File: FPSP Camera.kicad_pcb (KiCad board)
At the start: 4 copper layers, 85.7 x 31.1 mm, 73 parts, among them J1 Conn_01x24_Socket, J2 Conn_01x02, J3 Conn_02x07_Counter_Clockwise, J4 Conn_02x07_Counter_Clockwise, U1 ICM-45686, U3 RP2350_60QFN, U4 TLV75533PDRV, U5 TLV73328PDRV, U6 TLV73315PDRV, Y1 SiT8008xx-1x-xxE

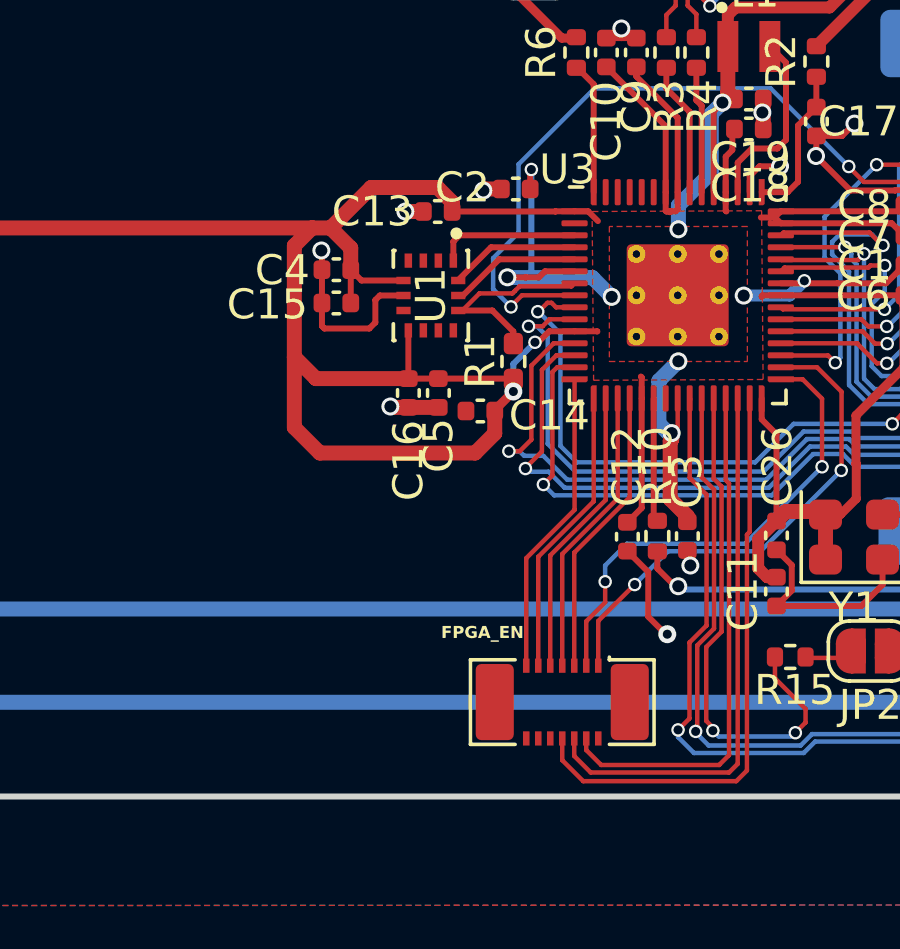
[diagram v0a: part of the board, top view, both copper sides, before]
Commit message: GPIO_1 added
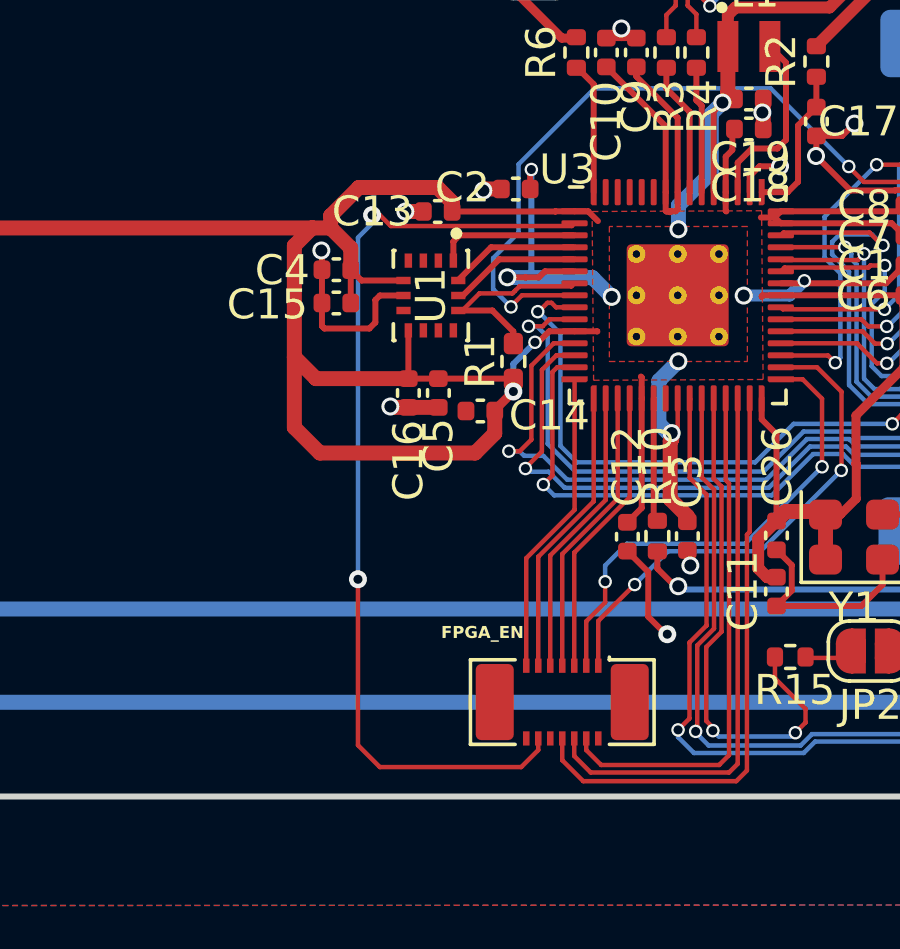
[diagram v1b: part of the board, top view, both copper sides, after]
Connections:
- J4 pad 12: unconnected-(J4-Pin_12-Pad12) -> POSITION_OUT_1
- J4 pad 3: POSITION_OUT_1 -> FPGA_CTRL
- U3 pad 2: /GPIO0_1 -> POSITION_OUT_1
- U3 pad 31: POSITION_OUT_1 -> FPGA_CTRL
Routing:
- net FPGA_CTRL: track 0.00 -> 16.1 mm, vias 0 -> 2
- net POSITION_OUT_1: track 16.1 -> 31.7 mm
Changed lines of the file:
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@@
 			(layers "F.Cu" "F.Mask" "F.Paste")
 			(roundrect_rratio 0.25)
-			(net "/GPIO0_1")
+			(net "POSITION_OUT_1")
 			(pinfunction "GPIO0_2")
 			(pintype "bidirectional")
@@
 			(chamfer_ratio 0.25)
 			(chamfer bottom_left)
-			(net "POSITION_OUT_1")
+			(net "FPGA_CTRL")
 			(pinfunction "GPIO19_31")
 			(pintype "bidirectional")
@@
 			(size 0.22 0.475)
 			(layers "F.Cu" "F.Mask" "F.Paste")
-			(net "POSITION_OUT_1")
+			(net "FPGA_CTRL")
 			(pinfunction "Pin_3_3")
 			(pintype "passive")
@@
 			(size 0.22 0.475)
 			(layers "F.Cu" "F.Mask" "F.Paste")
-			(net "unconnected-(J4-Pin_12-Pad12)")
+			(net "POSITION_OUT_1")
 			(pinfunction "Pin_12_12")
-			(pintype "passive+no_connect")
+			(pintype "passive")
 		)
 		(pad "13" smd rect
@@
 	)
 	(segment
+		(start 56.272265 26.719144)
+		(end 58.892264 26.719144)
+		(width 0.5)
+		(layer "F.Cu")
+		(net "+3.3V")
+	)
+	(segment
 		(start 66.622265 27.519144)
 		(end 66.645231 27.54211)
@@
 	)
 	(segment
+		(start 58.892264 26.719144)
+		(end 59.382265 27.209145)
+		(width 0.5)
+		(layer "F.Cu")
+		(net "+3.3V")
+	)
+	(segment
 		(start 58.922265 33.089144)
 		(end 57.922265 33.089144)
@@
 	)
 	(segment
-		(start 59.382265 27.209145)
-		(end 59.382265 27.519144)
-		(width 0.5)
-		(layer "F.Cu")
-		(net "+3.3V")
-	)
-	(segment
 		(start 73.412265 20.119144)
 		(end 71.522265 22.009144)
@@
 	)
 	(segment
-		(start 56.68234 26.719144)
-		(end 58.892264 26.719144)
-		(width 0.5)
-		(layer "F.Cu")
-		(net "+3.3V")
-	)
-	(segment
-		(start 55.33334 28.068144)
-		(end 56.68234 26.719144)
-		(width 0.5)
-		(layer "F.Cu")
-		(net "+3.3V")
-	)
-	(segment
 		(start 39.222265 30.869144)
 		(end 39.222265 30.876644)
@@
 	)
 	(segment
-		(start 58.892264 26.719144)
-		(end 59.382265 27.209145)
-		(width 0.5)
-		(layer "F.Cu")
-		(net "+3.3V")
-	)
-	(segment
 		(start 31.122265 30.019144)
 		(end 31.472265 29.669144)
@@
 	)
 	(segment
+		(start 59.382265 27.209145)
+		(end 59.382265 27.519144)
+		(width 0.5)
+		(layer "F.Cu")
+		(net "+3.3V")
+	)
+	(segment
 		(start 62.822265 27.519144)
 		(end 59.382265 27.519144)
@@
 	)
 	(segment
+		(start 55.33334 28.068144)
+		(end 55.33334 27.658069)
+		(width 0.5)
+		(layer "F.Cu")
+		(net "+3.3V")
+	)
+	(segment
 		(start 70.3375 27.5125)
 		(end 70.130856 27.719144)
@@
 	)
 	(segment
+		(start 55.33334 27.658069)
+		(end 56.272265 26.719144)
+		(width 0.5)
+		(layer "F.Cu")
+		(net "+3.3V")
+	)
+	(segment
 		(start 80.422265 24.769144)
 		(end 80.422265 21.869144)
@@
 	)
 	(segment
-		(start 64.482265 39.859144)
-		(end 64.482265 40.549144)
+		(start 56.242265 39.779144)
+		(end 56.242265 45.309144)
 		(width 0.15)
 		(layer "F.Cu")
@@
 	)
 	(segment
-		(start 64.482265 40.549144)
-		(end 63.852265 41.179144)
+		(start 56.712265 27.639144)
+		(end 56.972265 27.639144)
 		(width 0.15)
 		(layer "F.Cu")
@@
 	)
 	(segment
-		(start 70.3375 33.1125)
-		(end 71.065621 33.1125)
+		(start 61.684765 46.039144)
+		(end 62.252265 45.471644)
 		(width 0.15)
 		(layer "F.Cu")
@@
 	)
 	(segment
-		(start 71.065621 33.1125)
-		(end 71.712265 33.759144)
+		(start 62.252265 45.471644)
+		(end 62.252265 45.084144)
 		(width 0.15)
 		(layer "F.Cu")
@@
 	)
 	(segment
-		(start 63.852265 41.179144)
-		(end 63.852265 42.659144)
+		(start 63.370856 28.004144)
+		(end 63.4625 27.9125)
 		(width 0.15)
 		(layer "F.Cu")
@@
 	)
 	(segment
-		(start 71.712265 33.759144)
-		(end 71.712265 36.029144)
+		(start 56.242265 45.309144)
+		(end 56.972265 46.039144)
+		(width 0.15)
+		(layer "F.Cu")
+		(net "POSITION_OUT_1")
+	)
+	(segment
+		(start 56.972265 46.039144)
+		(end 61.684765 46.039144)
+		(width 0.15)
+		(layer "F.Cu")
+		(net "POSITION_OUT_1")
+	)
+	(segment
+		(start 56.972265 27.639144)
+		(end 57.337265 28.004144)
+		(width 0.15)
+		(layer "F.Cu")
+		(net "POSITION_OUT_1")
+	)
+	(segment
+		(start 57.337265 28.004144)
+		(end 63.370856 28.004144)
 		(width 0.15)
 		(layer "F.Cu")
@@
 	)
 	(via
-		(at 64.482265 39.859144)
-		(size 0.45)
+		(at 56.242265 39.779144)
+		(size 0.6)
 		(drill 0.3)
 		(layers "F.Cu" "B.Cu")
@@
 	)
 	(via
-		(at 71.712265 36.029144)
-		(size 0.45)
+		(at 56.712265 27.639144)
+		(size 0.6)
 		(drill 0.3)
 		(layers "F.Cu" "B.Cu")
@@
 	)
 	(segment
-		(start 69.147265 38.594144)
-		(end 65.207265 38.594144)
+		(start 56.712265 27.639144)
+		(end 56.712265 27.919144)
 		(width 0.15)
 		(layer "B.Cu")
@@
 	)
 	(segment
-		(start 71.712265 36.029144)
-		(end 69.147265 38.594144)
+		(start 56.242265 28.389144)
+		(end 56.242265 39.779144)
 		(width 0.15)
 		(layer "B.Cu")
@@
 	)
 	(segment
-		(start 65.207265 38.594144)
-		(end 64.482265 39.319144)
-		(width 0.15)
-		(layer "B.Cu")
-		(net "POSITION_OUT_1")
-	)
-	(segment
-		(start 64.482265 39.319144)
-		(end 64.482265 39.859144)
+		(start 56.712265 27.919144)
+		(end 56.242265 28.389144)
 		(width 0.15)
 		(layer "B.Cu")
@@
 		(net "DGND")
 	)
+	(segment
+		(start 64.482265 39.859144)
+		(end 64.482265 40.549144)
+		(width 0.15)
+		(layer "F.Cu")
+		(net "FPGA_CTRL")
+	)
+	(segment
+		(start 64.482265 40.549144)
+		(end 63.852265 41.179144)
+		(width 0.15)
+		(layer "F.Cu")
+		(net "FPGA_CTRL")
+	)
+	(segment
+		(start 70.3375 33.1125)
+		(end 71.065621 33.1125)
+		(width 0.15)
+		(layer "F.Cu")
+		(net "FPGA_CTRL")
+	)
+	(segment
+		(start 71.065621 33.1125)
+		(end 71.712265 33.759144)
+		(width 0.15)
+		(layer "F.Cu")
+		(net "FPGA_CTRL")
+	)
+	(segment
+		(start 63.852265 41.179144)
+		(end 63.852265 42.659144)
+		(width 0.15)
+		(layer "F.Cu")
+		(net "FPGA_CTRL")
+	)
+	(segment
+		(start 71.712265 33.759144)
+		(end 71.712265 36.029144)
+		(width 0.15)
+		(layer "F.Cu")
+		(net "FPGA_CTRL")
+	)
+	(via
+		(at 64.482265 39.859144)
+		(size 0.45)
+		(drill 0.3)
+		(layers "F.Cu" "B.Cu")
+		(net "FPGA_CTRL")
+	)
+	(via
+		(at 71.712265 36.029144)
+		(size 0.45)
+		(drill 0.3)
+		(layers "F.Cu" "B.Cu")
+		(net "FPGA_CTRL")
+	)
+	(segment
+		(start 69.147265 38.594144)
+		(end 65.207265 38.594144)
+		(width 0.15)
+		(layer "B.Cu")
+		(net "FPGA_CTRL")
+	)
+	(segment
+		(start 71.712265 36.029144)
+		(end 69.147265 38.594144)
+		(width 0.15)
+		(layer "B.Cu")
+		(net "FPGA_CTRL")
+	)
+	(segment
+		(start 65.207265 38.594144)
+		(end 64.482265 39.319144)
+		(width 0.15)
+		(layer "B.Cu")
+		(net "FPGA_CTRL")
+	)
+	(segment
+		(start 64.482265 39.319144)
+		(end 64.482265 39.859144)
+		(width 0.15)
+		(layer "B.Cu")
+		(net "FPGA_CTRL")
+	)
 	(zone
 		(net "+5V")
@@
 		(polygon
 			(pts
-				(xy 56.522265 27.969144) (xy 56.522265 32.569144) (xy 60.922265 32.569144) (xy 60.922265 27.969144)
+				(xy 56.522265 27.939144) (xy 56.522265 32.569144) (xy 60.922265 32.569144) (xy 60.922265 27.939144)
 			)
 		)

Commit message: layout refined
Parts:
- removed D4: LED, Diode_SMD:D_0603_1608Metric
- removed R21: 10k, Resistor_SMD:R_0402_1005Metric
- added TP3: 1V5, TestPoint:TestPoint_Pad_D1.0mm, F.Cu at (29.4, 36.1)
- TP1: value TestPoint -> 1V1
- moved C11 2.12 mm to (71.2, 38.3)
- moved Y1 0.73 mm to (73.5, 38.4)
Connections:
- J3 pad 15: AGND -> (no net)
- J3 pad 16: AGND -> (no net)
- J4 pad 15: AGND -> (no net)
- J4 pad 16: AGND -> (no net)
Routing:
- net /VREG_LX_1: track 6.24 -> 0.00 mm
- net +3.3V: track 165.4 -> 160.9 mm
- net AGND: track 49.7 -> 47.6 mm, vias 23 -> 142
- net Net-(D4-A): track 1.55 -> 0.00 mm
- net +1V5: track 74.0 -> 75.5 mm
- net DATA2_1: track 11.5 -> 12.1 mm
- net DATA3_1: track 11.9 -> 12.5 mm
- net DATA6_1: track 15.3 -> 15.9 mm
- net /XIN_mem1: track 15.2 -> 14.7 mm
- added copper zone on F.Cu, net /VREG_LX_1
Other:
- board text added: "1V5"
- board text added: "2V8"
- board text added: "3V3"
- board text removed: "1.5"
- board text removed: "2.8"
- board text removed: "3.3"

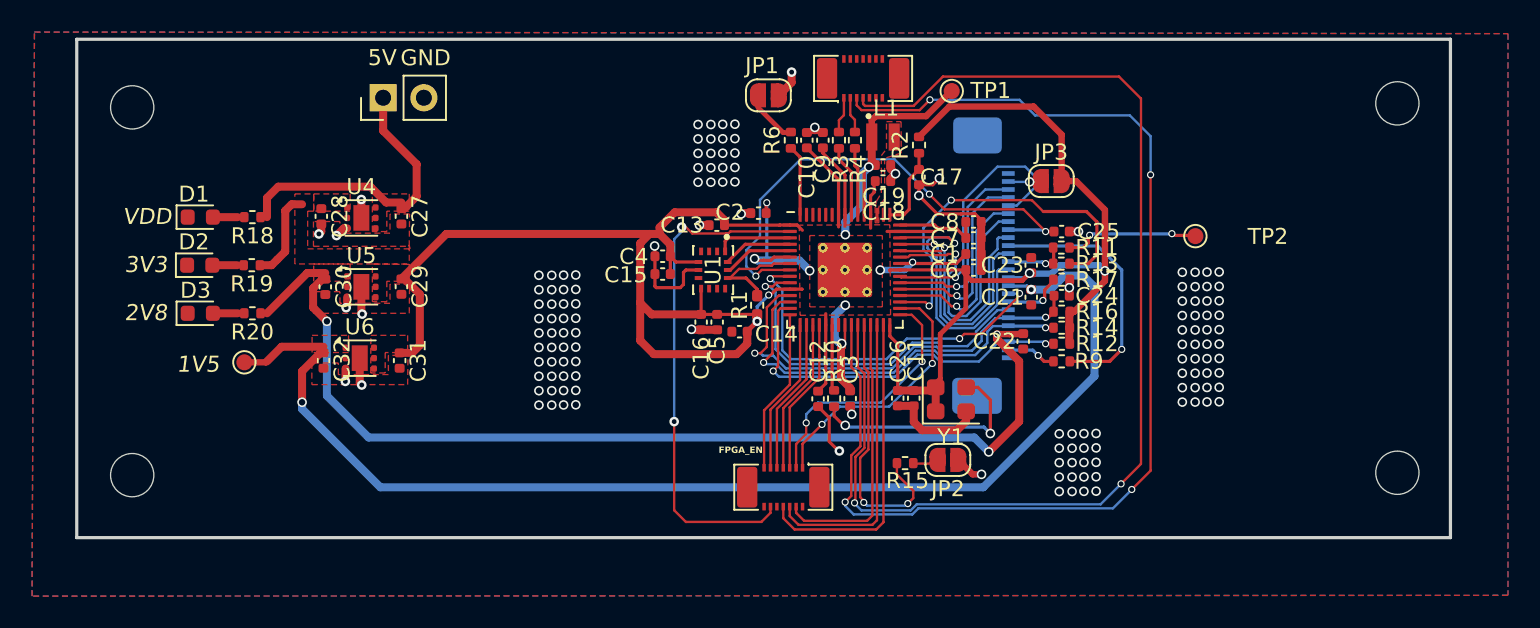
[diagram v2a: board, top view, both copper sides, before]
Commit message: Rpi Buck layout refined
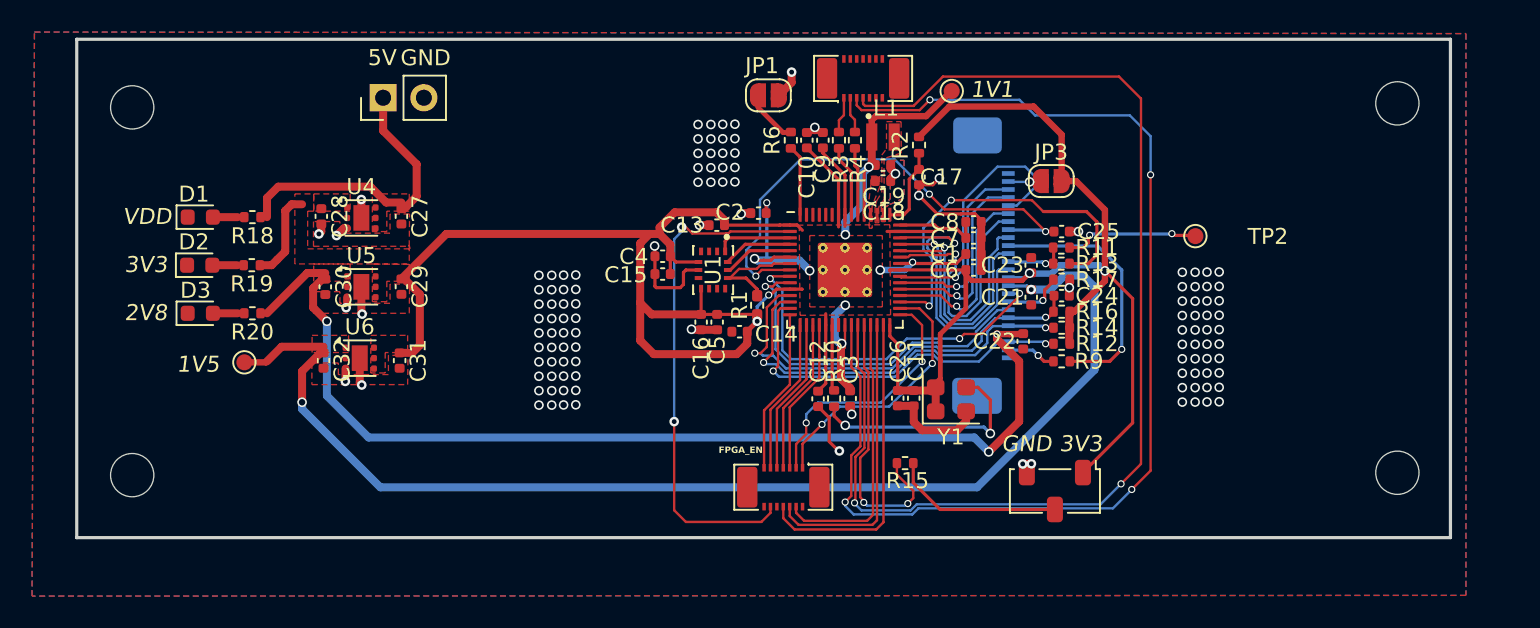
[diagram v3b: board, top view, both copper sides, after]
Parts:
- removed JP2: SolderJumper_2_Open, Jumper:SolderJumper-2_P1.3mm_Open_RoundedPad1.0x1.5mm
- added SW1: SW_Nidec_CAS-120A1, Button_Switch_SMD:Nidec_Copal_CAS-120A, F.Cu at (80.0, 44.1)
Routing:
- net +3.3V: track 160.9 -> 172.5 mm
- net Net-(SW1-B): track 1.56 -> 10.8 mm
- net AGND: track 47.6 -> 45.8 mm, vias 142 -> 123
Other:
- board text added: "1V1"

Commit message: push button added; IMU updated
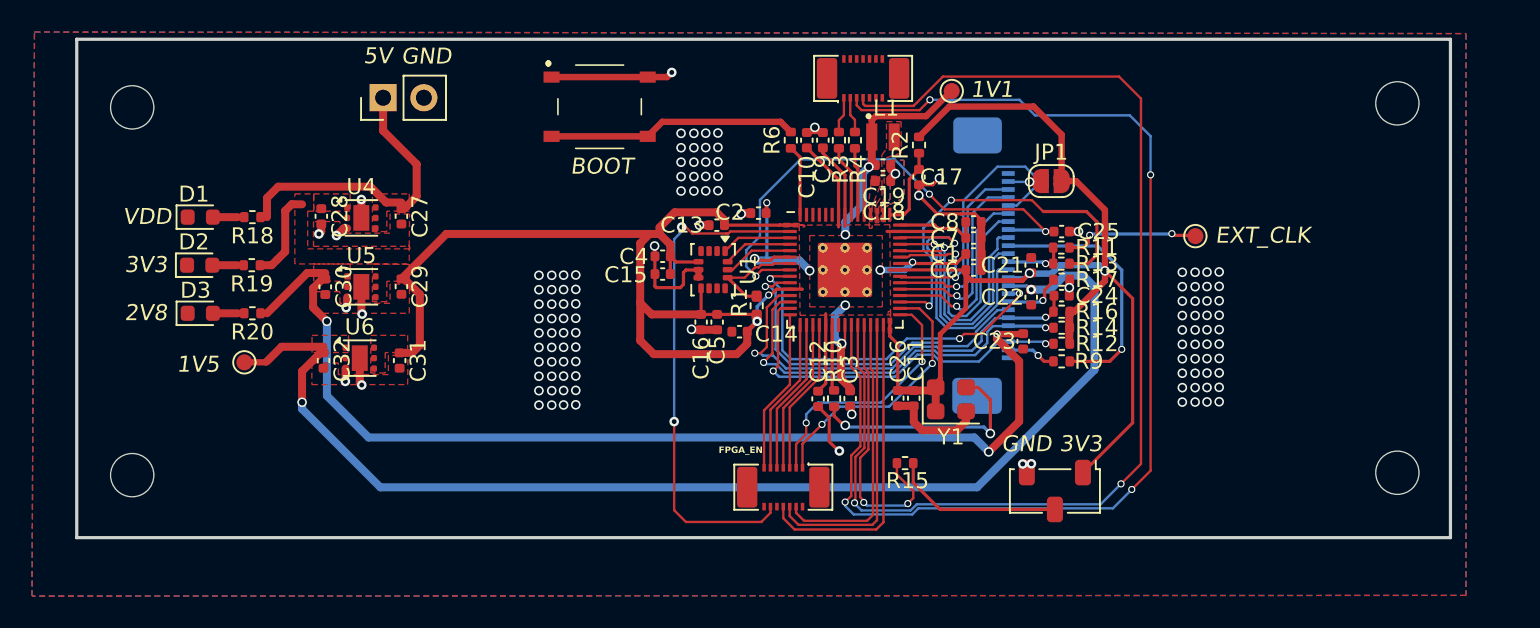
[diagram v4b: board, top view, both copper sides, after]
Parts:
- removed the JP1 at (62.1, 19.4)
- added SW1: PTS526_SM15_SMTR2_LFS, PTS526_SM15_SMTR2_LFS:PTS526SM15SMTR2LFS, F.Cu at (51.6, 20.1)
- U1: value ICM-45686 -> LSM6DSL; footprint ICM_45686:IC_ICM-45686 -> Package_LGA:LGA-14_3x2.5mm_P0.5mm_LayoutBorder3x4y
- renumbered C23 to C21, C21 to C22, C22 to C23, JP3 to JP1, SW1 to SW2
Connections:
- net /IMU_SDI renamed /IMU_SDA
- net SWCLK_1 renamed /SWCLK_1
- net SWD_1 renamed /SWD_1
- U1 pad 7: unconnected-(U1-RESV/NC-Pad7) -> AGND
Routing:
- net /~{USB_BOOT_1}: track 3.45 -> 15.6 mm
- net AGND: track 45.8 -> 52.1 mm
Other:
- board text added: "BOOT"
- board text added: "EXT_CLK"

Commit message: connector board pin order updated
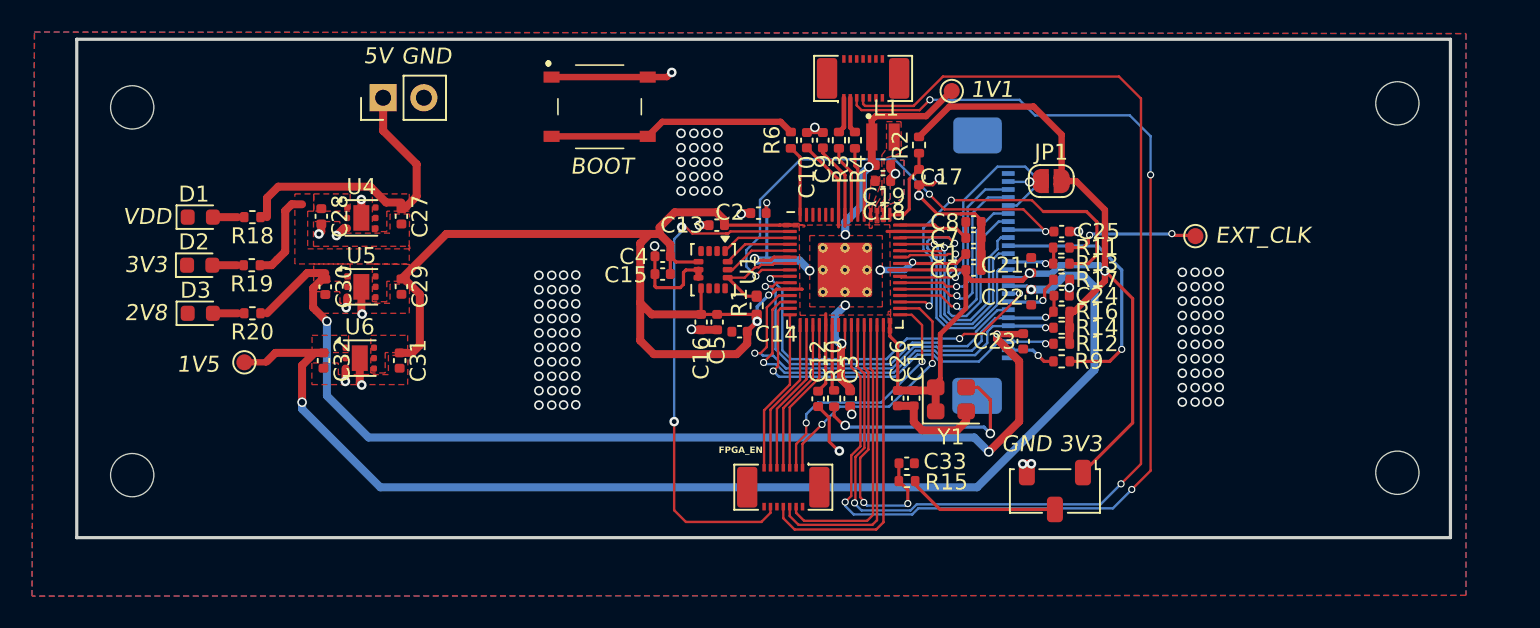
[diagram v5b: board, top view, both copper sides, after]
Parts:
- added C33: 100n, Capacitor_SMD:C_0402_1005Metric, F.Cu at (70.8, 42.4)
- R15: value 1k -> 10k
- moved R15 1.13 mm to (70.8, 43.5)
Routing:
- net Net-(SW2-B): track 10.8 -> 9.58 mm

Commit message: new connector footprint updated
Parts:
- removed J3: Conn_02x07_Counter_Clockwise, Connector_Molex:Molex_SlimStack_502426-1410_2x07_P0.40mm_Vertical
- added J5: Conn_02x06_Top_Bottom, 5035481222:CON_5035481222, F.Cu at (67.8, 18.3)
- J4: value Conn_02x07_Counter_Clockwise -> Conn_02x06_Top_Bottom; footprint Connector_Molex:Molex_SlimStack_502426-1410_2x07_P0.40mm_Vertical -> 5035481222:CON_5035481222
- moved J4 0.20 mm to (62.9, 43.9), turned to 180 degrees
- renumbered C33 to C24, C24 to C25, C25 to C26, C26 to C27, C27 to C28, C28 to C29, C29 to C30, C30 to C31, C31 to C32, C32 to C33
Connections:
- J4 pad 1: HREF_OUT -> FPGA_CTRL
- J4 pad 10: unconnected-(J4-Pin_10-Pad10) -> POSITION_OUT_CLK
- J4 pad 11: IMAGE_OUT_1 -> POSITION_OUT_1
- J4 pad 12: POSITION_OUT_1 -> AGND
- J4 pad 2: unconnected-(J4-Pin_2-Pad2) -> IMAGE_OUT_4
- J4 pad 3: FPGA_CTRL -> IMAGE_OUT_3
- J4 pad 4: IMAGE_CLK -> IMAGE_OUT_2
- J4 pad 5: IMAGE_OUT_4 -> IMAGE_OUT_1
- J4 pad 6: VSYNC_OUT -> FPGA_EN
- J4 pad 7: IMAGE_OUT_3 -> HREF_OUT
- J4 pad 8: POSITION_OUT_CLK -> IMAGE_CLK
- J4 pad 9: IMAGE_OUT_2 -> VSYNC_OUT
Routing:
- net AGND: track 52.1 -> 58.3 mm, vias 123 -> 125
- net HREF_OUT: track 16.7 -> 19.2 mm
